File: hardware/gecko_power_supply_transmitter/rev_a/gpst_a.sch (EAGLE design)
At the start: 7 parts, among them J1 EPIC-PROG-POGO-NO-LEGS, J2 GECKO_POWER_SUPPLY_CONN, U1 EPIC-CORE_A

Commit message: no longer using epic
cc2538 and chip antenna ftw
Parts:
- removed ANT1: PIFA-2.4GHZ, epic:PIFA-2.4GHZ
- added A1: FRACTUS-2.4GHZ-FR05-S1-N-0-001, chips:FRACTUS-2.4GHZ-FR05-S1-N-0-001
- added B1: 2450BM15A0002, chips:2450BM15A0002
- added C10, C11, C12, C14, C15, C8, C9: 100nF, passives:CAPACITOR
- added C13: 220pF, passives:CAPACITOR
- added C16, C17, C7: 1uF, passives:CAPACITOR
- added C3, C4: 0.1uF, rcl:C-EUC0603
- added C5, C6: 12pF, passives:CAPACITOR
- added R2: (no value), passives:RESISTOR
- added U2: FM25LB, chips:FM25LB
- added U3: MSP430FR5969, chips:MSP430FR5969
- added U4: CC2538, chips:CC2538
- added X1: EPSON-FA-128, crystals:EPSON-FA-128
- U1: value EPIC-CORE_A -> DS2411; device epic:EPIC-CORE_A -> chips:DS2411
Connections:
- removed net N$1: ANT1.RFOUT, U1.RFOUT
- removed net RFGND: ANT1.RFGND@2, ANT1.RFGND@3, U1.RFGND1, U1.RFGND2
- new net N$10: C6.1, U4.XOSC32M_Q2, X1.2
- new net N$15: C16.1, C17.1, U4.DCOUPL1, U4.DCOUPL2
- new net N$5: B1.BAL_P, U4.RF_P
- new net N$6: B1.BAL_N, U4.RF_N
- new net N$7: A1.ANTENNA, B1.ANT
- new net N$9: C5.1, U4.XOSC32M_Q1, X1.1
- net !RST: no longer U1.RST/NMI
- net GND: now also B1.GND, C10.2, C11.2, C12.2, C13.2, C14.2, C15.2, C16.2, C17.2, C3.2, C5.2, C6.2, C7.2, C8.2, C9.2, U2.VSS, U4.GND, X1.GND; no longer U1.AGND, U1.GND1, U1.GND2, U1.GND3
- net RX: no longer U1.UART1RX
- net TCK: no longer U1.TCK
- net TX: no longer U1.UART1TX
- net VCC: now also C10.1, C11.1, C12.1, C13.1, C14.1, C15.1, C3.1, C7.1, C8.1, C9.1, U2.VDD, U4.AVDD, U4.AVDD_GUARD, U4.DVDD; no longer U1.AVDD, U1.DVDD
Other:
- note added: "PIN10"
- note added: "PIN15"
- note added: "PIN24"
- note added: "PIN33"
- note added: "PIN36"
- note added: "PIN40"
- note added: "PIN43"
- note added: "PIN55"

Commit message: routed except for vcc
the transmitter board is coming along nicely.
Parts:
- removed C3, C4: 0.1uF, rcl:C-EUC0603
- removed J1: EPIC-PROG-POGO-NO-LEGS, epic:EPIC-PROG-POGO-NO-LEGS
- removed U3: MSP430FR5969, chips:MSP430FR5969
- added C18: 2.2uF, passives:CAPACITOR
- added J3: TC2030-CTX-NL, connector:TC2030-CTX-NL
- added Q2: MOSFET-NCHANNELXFDN-3, fets:MOSFET-NCHANNELXFDN-3
- added R1, R3, R4: 4.7k, passives:RESISTOR
- added R5: 2.2k, passives:RESISTOR
- added R6: 4.7M, passives:RESISTOR
- added R7: 56k, passives:RESISTOR
- C1: device rcl:C-EUC0603 -> passives:CAPACITOR
- C2: value 0.1uF -> 1nF; device rcl:C-EUC0603 -> passives:CAPACITOR
- R2: value (none) -> 2.2k
- U2: value FM25LB -> FM25LBTDFN-8; device chips:FM25LB -> chips:FM25LBTDFN-8; DIGIKEY (none) -> FM25L04B-DGRA-ND; MOUSER (none) -> 877-FM25L04B-DG
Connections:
- removed net !RST: J1.RST#
- removed net RX: J1.RX1
- removed net TX: J1.TX1
- new net !FRAM_CS: R1.1, U2.!CS, U4.PC5
- new net !FRAM_HOLD: R3.1, U2.!HOLD, U4.PC1
- new net !FRAM_WP: R4.1, U2.!WP, U4.PC6
- new net !RESET: J3.!RESET, R2.1
- new net DS2411: R5.1, U1.I/O, U4.PB0
- new net MISO: U2.SO, U4.PC4
- new net MOSI: U2.SI, U4.PC3
- new net N$1: C2.1, R2.2, U4.!RESET
- new net N$11: C18.1, Q2.S, R6.2
- new net SCK: U2.SCK, U4.PC2
- new net TDI: U4.PB6/JTAG-TDI
- new net TDO: J3.TDO, U4.PB7/JTAG-TDO
- new net TIME_CTL: Q2.G, U4.PC0
- new net TMS: J3.TMS, U4.JTAG_TMS
- net GND: now also C18.2, C2.2, J3.GND, R6.1, R7.2, U1.GND; no longer C3.2, J1.GND
- net N$8: now also R7.1, U4.R_BIAS; no longer C2.2
- net TCK: now also J3.TCK, U4.JTAG_TCK; no longer J1.TCK
- net VCC: now also J3.VCC, Q2.D, R1.2, R3.2, R4.2, R5.2, U1.VCC; no longer C2.1, C3.1, J1.VDD

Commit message: getting closer with vcc
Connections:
- removed net N$11: C18.1, Q2.S, R6.2
- new net V_TIMER: C18.1, Q2.S, R6.2, U4.PA0/ROM-UART-RX
- net SHD: now also U4.PC7
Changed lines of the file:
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@@
 <setting verticaltext="up"/>
 </settings>
-<grid distance="0.1" unitdist="inch" unit="inch" style="lines" multiple="1" display="yes" altdistance="0.01" altunitdist="inch" altunit="inch"/>
+<grid distance="0.1" unitdist="inch" unit="inch" style="lines" multiple="1" display="no" altdistance="0.01" altunitdist="inch" altunit="inch"/>
 <layers>
 <layer number="1" name="Top" color="4" fill="1" visible="no" active="no"/>
@@
 </segment>
 </net>
-<net name="N$11" class="0">
+<net name="V_TIMER" class="0">
 <segment>
 <wire x1="208.28" y1="68.58" x2="208.28" y2="66.04" width="0.1524" layer="91"/>
@@
 <junction x="208.28" y="66.04"/>
 <pinref part="Q2" gate="G$1" pin="S"/>
+<wire x1="203.2" y1="66.04" x2="198.12" y2="66.04" width="0.1524" layer="91"/>
+<junction x="203.2" y="66.04"/>
+<label x="198.12" y="66.04" size="1.27" layer="95" rot="R180" xref="yes"/>
+</segment>
+<segment>
+<pinref part="U4" gate="G$1" pin="PA0/ROM-UART-RX"/>
+<wire x1="27.94" y1="101.6" x2="25.4" y2="101.6" width="0.1524" layer="91"/>
+<label x="25.4" y="101.6" size="1.27" layer="95" rot="R180" xref="yes"/>
 </segment>
 </net>
@@
 <label x="35.56" y="162.56" size="1.27" layer="95" xref="yes"/>
 </segment>
-</net>
+<segment>
+<pinref part="U4" gate="G$1" pin="PC7"/>
+<wire x1="27.94" y1="38.1" x2="25.4" y2="38.1" width="0.1524" layer="91"/>
+<label x="25.4" y="38.1" size="1.27" layer="95" rot="R180" xref="yes"/>
+</segment>
+</net>

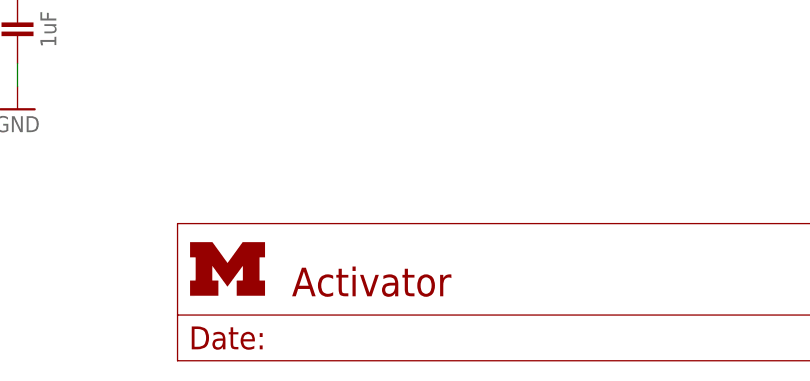
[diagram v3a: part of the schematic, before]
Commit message: got rf routed
added silkscreen
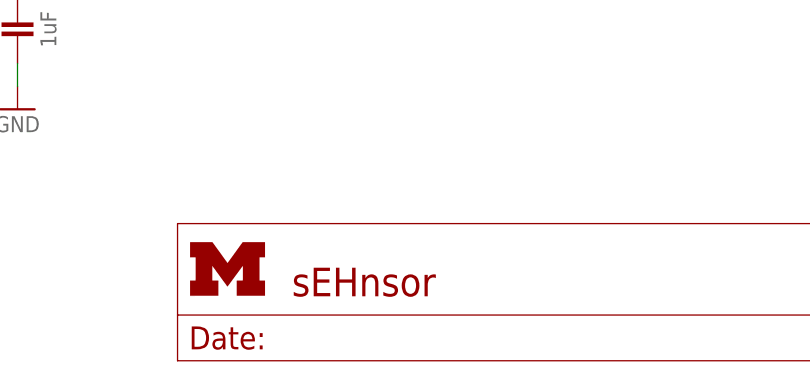
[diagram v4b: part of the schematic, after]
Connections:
- net N$5 renamed RF_P
- net N$6 renamed RF_N
- net N$7 renamed ANTENNA
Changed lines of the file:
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@@
 <?xml version="1.0" encoding="utf-8"?>
 <!DOCTYPE eagle SYSTEM "eagle.dtd">
-<eagle version="6.4">
+<eagle version="6.5.0">
 <drawing>
 <settings>
@@
 <attributes>
 <attribute name="REVISION" value="A"/>
-<attribute name="TITLE" value="Activator"/>
+<attribute name="TITLE" value="sEHnsor"/>
 </attributes>
 <variantdefs>
@@
 </busses>
 <nets>
-<net name="N$5" class="0">
+<net name="RF_P" class="0">
 <segment>
 <pinref part="U4" gate="G$1" pin="RF_P"/>
@@
 </segment>
 </net>
-<net name="N$6" class="0">
+<net name="RF_N" class="0">
 <segment>
 <pinref part="B1" gate="G$1" pin="BAL_N"/>
@@
 </segment>
 </net>
-<net name="N$7" class="0">
+<net name="ANTENNA" class="0">
 <segment>
 <pinref part="B1" gate="G$1" pin="ANT"/>

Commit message: bom and new pdfs
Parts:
- removed C17: 1uF, passives:CAPACITOR
- removed C18: 2.2uF, passives:CAPACITOR
- removed J3: TC2030-CTX-NL, connector:TC2030-CTX-NL
- added C3: 220pF, passives:CAPACITOR
- added C4: 1nF, passives:CAPACITOR
- added J1: GECKO_POWER_SUPPLY_CONN, gecko:GECKO_POWER_SUPPLY_CONN
- C1: value 0.1uF -> 12pF
- C10, C11, C12, C8, C9: value 100nF -> 0.1uF
- C13: value 220pF -> 1uF
- C14, C15: value 100nF -> 1uF
- C16: value 1uF -> 2.2uF
- C2: value 1nF -> 12pF
- C5, C6: value 12pF -> 0.1uF
- C7: value 1uF -> 0.1uF
- J2: value GECKO_POWER_SUPPLY_CONN -> TC2030-CTX-NL; device gecko:GECKO_POWER_SUPPLY_CONN -> connector:TC2030-CTX-NL
- R1: value 4.7k -> 2.2k
- R5: value 2.2k -> 4.7k
- R6: value 4.7M -> 56k
- R7: value 56k -> 4.7M
- renumbered Q2 to Q1, U4 to U3
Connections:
- net !FRAM_CS: now also R3.1; no longer R1.1
- net !FRAM_HOLD: now also R4.1; no longer R3.1
- net !FRAM_WP: now also R5.1; no longer R4.1
- net !RESET: now also J2.!RESET, R1.1; no longer J3.!RESET, R2.1
- net DS2411: now also R2.1; no longer R5.1
- net GND: now also C3.2, C4.2, J1.GND, R6.2, R7.1; no longer C17.2, C18.2, J3.GND, R6.1, R7.2
- net N$1: now also C4.1, R1.2; no longer C2.1, R2.2
- net N$10: now also C2.1; no longer C6.1
- net N$15: now also C14.1, C15.1; no longer C16.1, C17.1
- net N$8: now also R6.1; no longer R7.1
- net N$9: now also C1.1; no longer C5.1
- net OV: now also J1.OVERVOLT; no longer J2.OVERVOLT
- net SHD: now also J1.SHUTDOWN; no longer J2.SHUTDOWN
- net TCK: now also J2.TCK; no longer J3.TCK
- net TDO: now also J2.TDO; no longer J3.TDO
- net TMS: now also J2.TMS; no longer J3.TMS
- net TRIG: now also J1.TRIGGER; no longer J2.TRIGGER
- net VCAP: now also J1.VCAP; no longer J2.VCAP
- net VCC: now also C3.1, C5.1, C6.1, J1.VREG, J2.VCC, R2.2; no longer C1.1, C14.1, C15.1, J2.VREG, J3.VCC, R1.2
- net V_TIMER: now also C16.1, R7.2; no longer C18.1, R6.2
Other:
- moved on the sheet: C1, C10, C11, C12, C13, C14, C15, C16, C2, C5, C6, C7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
